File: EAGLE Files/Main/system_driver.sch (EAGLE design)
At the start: 11 parts

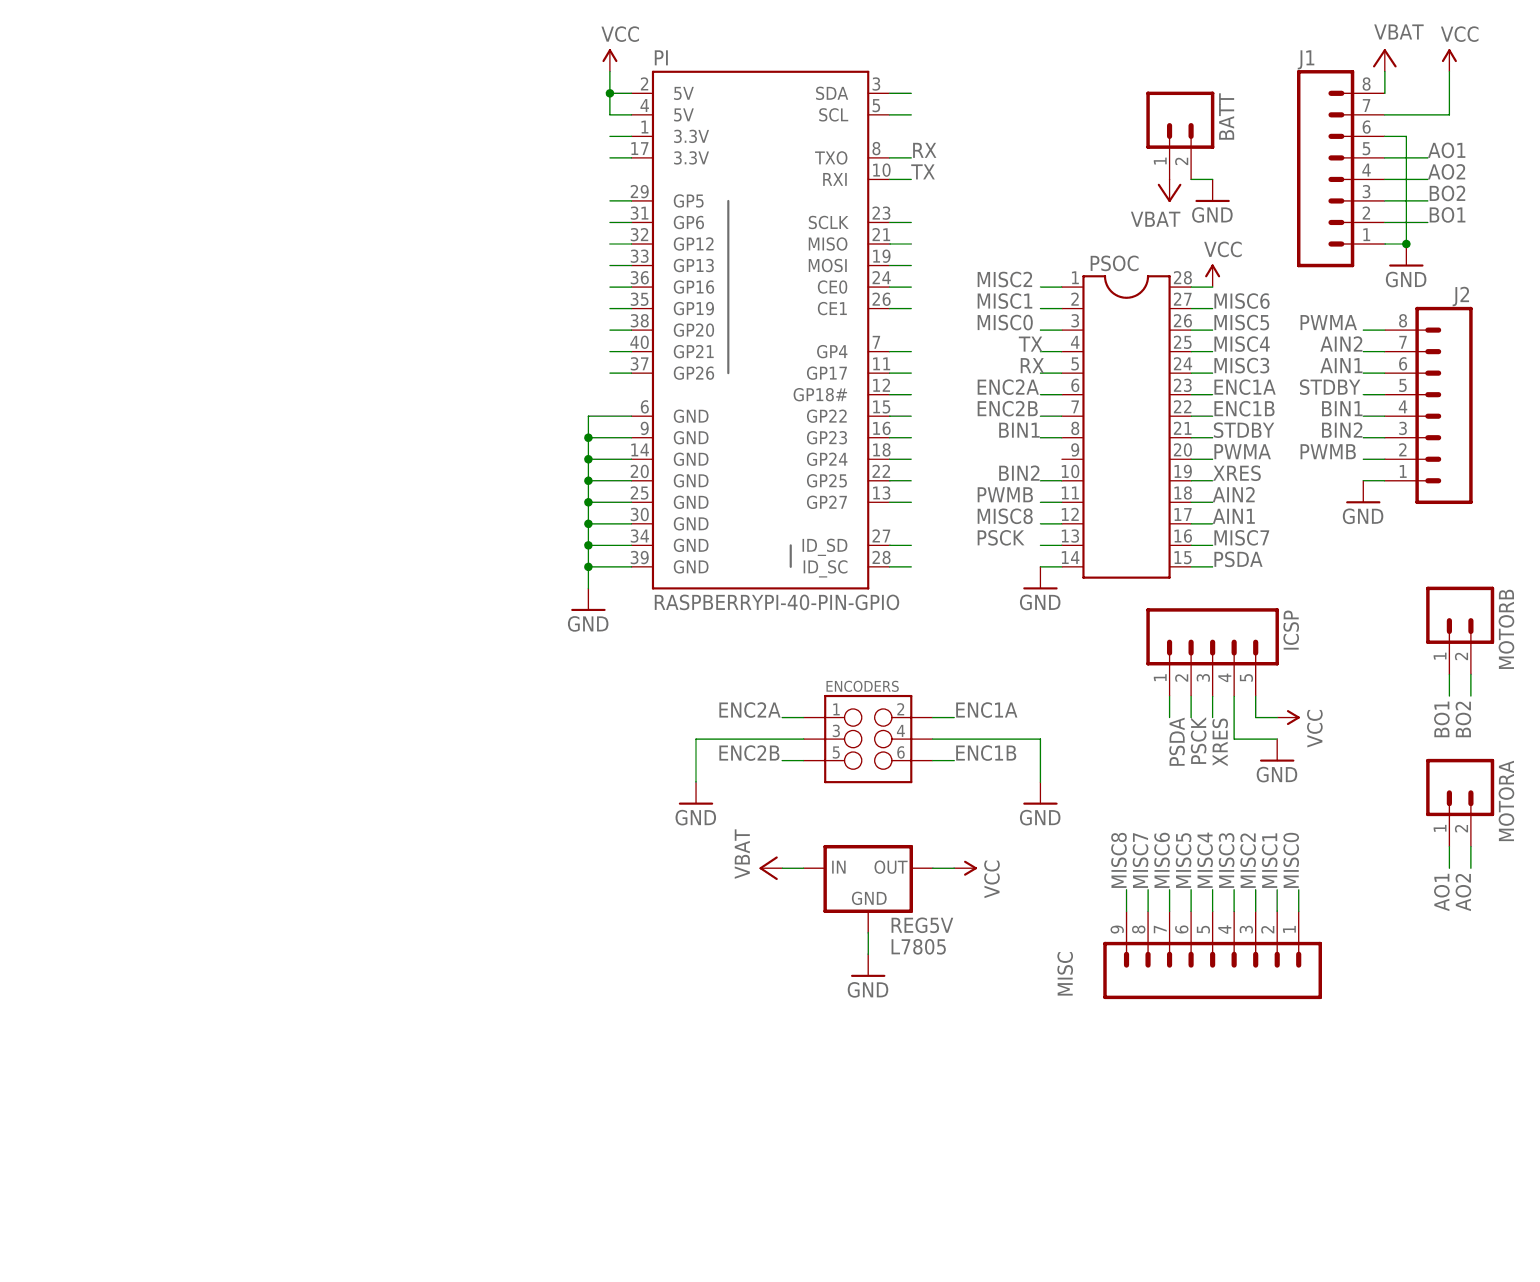
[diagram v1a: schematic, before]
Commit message: Updated PCB files, added PSoC code
Up to date PCB and schematic files for Robot 2's driver control board.
Also added the PSoC code files and project.
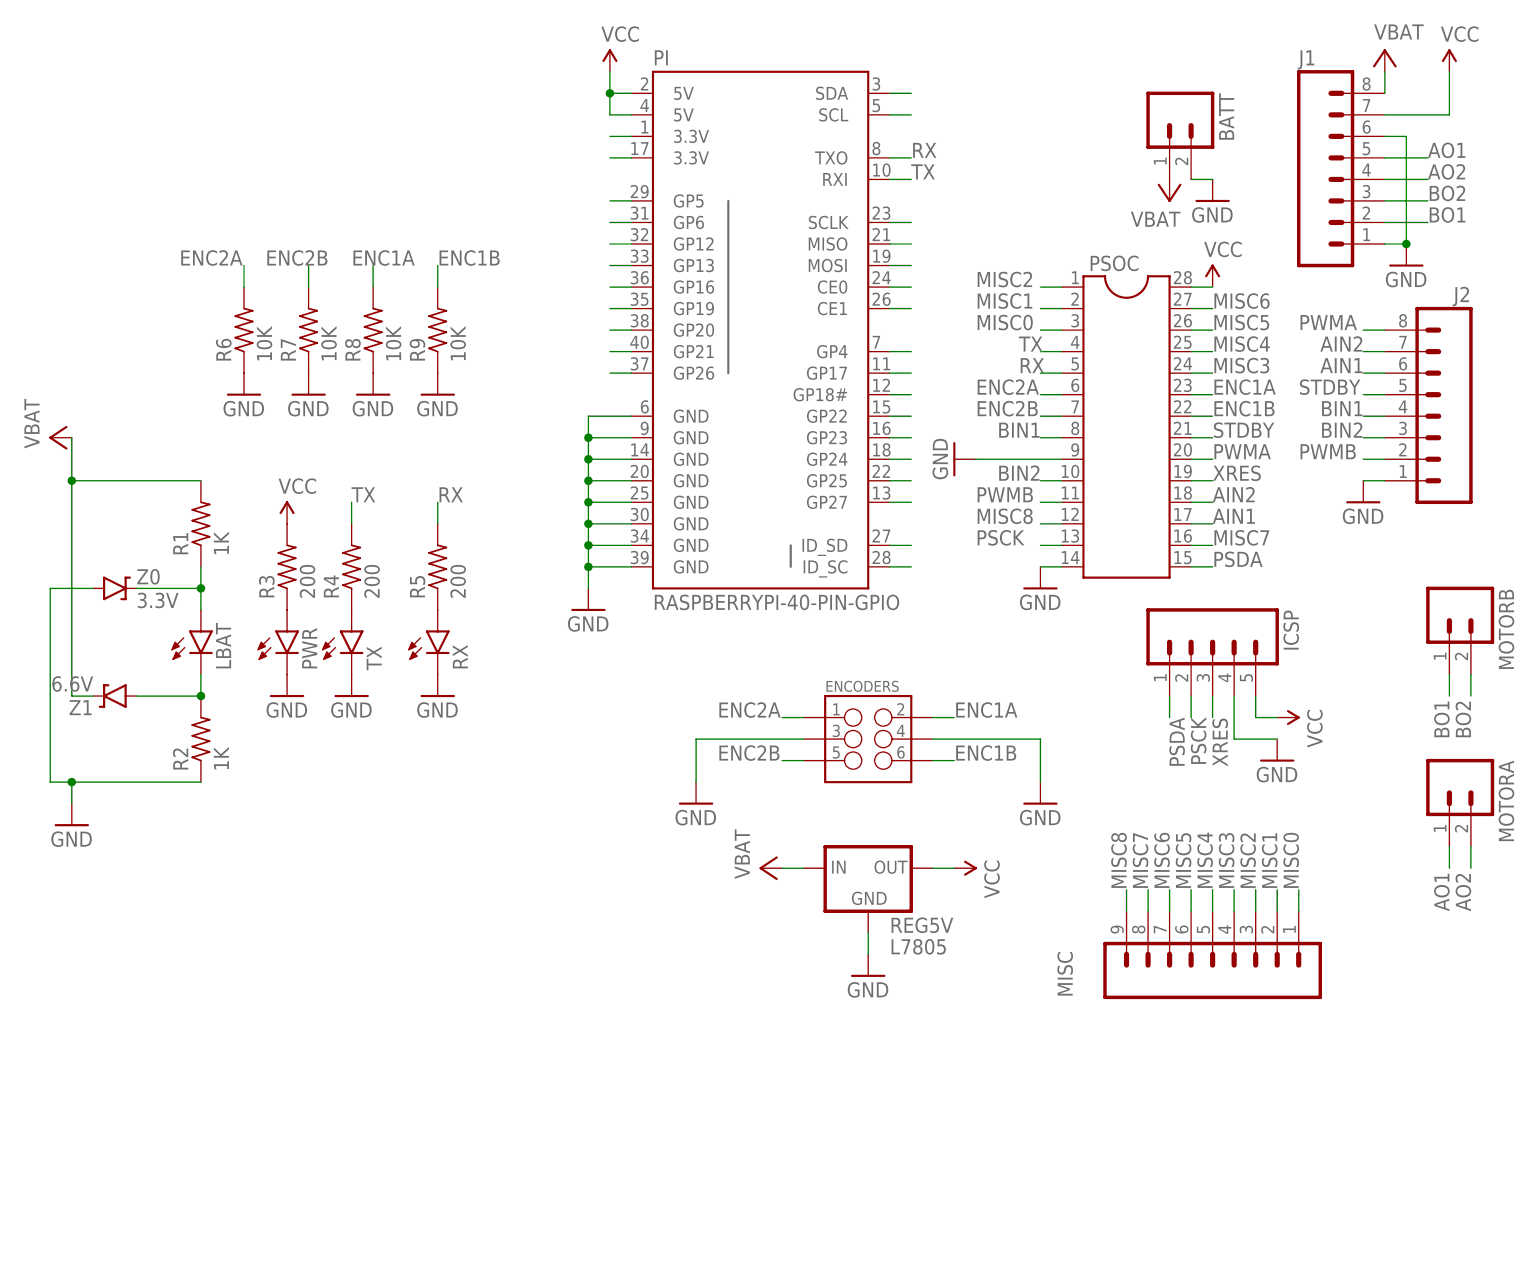
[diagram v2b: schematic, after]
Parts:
- added LBAT, PWR, RX, TX: (no value), SparkFun-LED:LED-FKIT-1206
- added R1, R2: 1K, resistor:R-US_M1206
- added R3, R4, R5: 200, resistor:R-US_M1206
- added R6, R7, R8, R9: 10K, resistor:R-US_M1206
- added Z0: 3.3V, SparkFun-DiscreteSemi:DIODE-ZENER16V
- added Z1: 6.6V, SparkFun-DiscreteSemi:DIODE-ZENER16V
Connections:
- new net N$1: LBAT.A, R1.1, Z0.C
- new net N$2: LBAT.C, R2.2, Z1.A
- new net N$3: PWR.A, R3.1
- new net N$4: R4.1, TX.A
- new net N$5: R5.1, RX.A
- net ENC1A: now also R8.2
- net ENC1B: now also R9.2
- net ENC2A: now also R6.2
- net ENC2B: now also R7.2
- net GND: now also PSOC.9, PWR.C, R2.1, R6.1, R7.1, R8.1, R9.1, RX.C, TX.C, Z0.A
- net RX: now also R5.2
- net TX: now also R4.2
- net V+: now also R1.2, Z1.C
- net VCC: now also R3.2
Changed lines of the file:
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@@
 <part name="VBAT2" library="supply2" deviceset="V+" device="" value="VBAT"/>
 <part name="SUPPLY7" library="SparkFun-Aesthetics" deviceset="VCC" device=""/>
+<part name="RX" library="SparkFun-LED" deviceset="LED" device="-FKIT-1206"/>
+<part name="TX" library="SparkFun-LED" deviceset="LED" device="-FKIT-1206"/>
+<part name="PWR" library="SparkFun-LED" deviceset="LED" device="-FKIT-1206"/>
+<part name="LBAT" library="SparkFun-LED" deviceset="LED" device="-FKIT-1206"/>
+<part name="R1" library="resistor" deviceset="R-US_" device="M1206" value="1K"/>
+<part name="R2" library="resistor" deviceset="R-US_" device="M1206" value="1K"/>
+<part name="Z1" library="SparkFun-DiscreteSemi" deviceset="DIODE-ZENER" device="16V" value="6.6V"/>
+<part name="Z0" library="SparkFun-DiscreteSemi" deviceset="DIODE-ZENER" device="16V" value="3.3V"/>
+<part name="GND7" library="SparkFun-Aesthetics" deviceset="GND" device=""/>
+<part name="VBAT3" library="supply2" deviceset="V+" device="" value="VBAT"/>
+<part name="R3" library="resistor" deviceset="R-US_" device="M1206" value="200"/>
+<part name="R4" library="resistor" deviceset="R-US_" device="M1206" value="200"/>
+<part name="R5" library="resistor" deviceset="R-US_" device="M1206" value="200"/>
+<part name="GND10" library="SparkFun-Aesthetics" deviceset="GND" device=""/>
+<part name="GND12" library="SparkFun-Aesthetics" deviceset="GND" device=""/>
+<part name="GND13" library="SparkFun-Aesthetics" deviceset="GND" device=""/>
+<part name="SUPPLY4" library="SparkFun-Aesthetics" deviceset="VCC" device=""/>
+<part name="GND14" library="SparkFun-Aesthetics" deviceset="GND" device=""/>
+<part name="GND15" library="SparkFun-Aesthetics" deviceset="GND" device=""/>
+<part name="GND16" library="SparkFun-Aesthetics" deviceset="GND" device=""/>
+<part name="GND17" library="SparkFun-Aesthetics" deviceset="GND" device=""/>
+<part name="GND18" library="SparkFun-Aesthetics" deviceset="GND" device=""/>
+<part name="R6" library="resistor" deviceset="R-US_" device="M1206" value="10K"/>
+<part name="R7" library="resistor" deviceset="R-US_" device="M1206" value="10K"/>
+<part name="R8" library="resistor" deviceset="R-US_" device="M1206" value="10K"/>
+<part name="R9" library="resistor" deviceset="R-US_" device="M1206" value="10K"/>
 </parts>
 <sheets>
@@
 <instance part="VBAT2" gate="1" x="-71.12" y="-15.24" rot="R90"/>
 <instance part="SUPPLY7" gate="G$1" x="-48.26" y="-15.24" rot="R270"/>
+<instance part="RX" gate="G$1" x="-109.22" y="12.7"/>
+<instance part="TX" gate="G$1" x="-119.38" y="12.7"/>
+<instance part="PWR" gate="G$1" x="-127" y="12.7"/>
+<instance part="LBAT" gate="G$1" x="-137.16" y="12.7"/>
+<instance part="R1" gate="G$1" x="-137.16" y="25.4" rot="R90"/>
+<instance part="R2" gate="G$1" x="-137.16" y="0" rot="R90"/>
+<instance part="Z1" gate="G$1" x="-147.32" y="5.08" rot="R180"/>
+<instance part="Z0" gate="G$1" x="-147.32" y="17.78"/>
+<instance part="GND7" gate="1" x="-152.4" y="-10.16"/>
+<instance part="VBAT3" gate="1" x="-154.94" y="35.56" rot="R90"/>
+<instance part="R3" gate="G$1" x="-127" y="20.32" rot="R90"/>
+<instance part="R4" gate="G$1" x="-119.38" y="20.32" rot="R90"/>
+<instance part="R5" gate="G$1" x="-109.22" y="20.32" rot="R90"/>
+<instance part="GND10" gate="1" x="-127" y="5.08"/>
+<instance part="GND12" gate="1" x="-119.38" y="5.08"/>
+<instance part="GND13" gate="1" x="-109.22" y="5.08"/>
+<instance part="SUPPLY4" gate="G$1" x="-127" y="25.4"/>
+<instance part="GND14" gate="1" x="-48.26" y="33.02" rot="R270"/>
+<instance part="GND15" gate="1" x="-109.22" y="40.64"/>
+<instance part="GND16" gate="1" x="-116.84" y="40.64"/>
+<instance part="GND17" gate="1" x="-124.46" y="40.64"/>
+<instance part="GND18" gate="1" x="-132.08" y="40.64"/>
+<instance part="R6" gate="G$1" x="-132.08" y="48.26" rot="R90"/>
+<instance part="R7" gate="G$1" x="-124.46" y="48.26" rot="R90"/>
+<instance part="R8" gate="G$1" x="-116.84" y="48.26" rot="R90"/>
+<instance part="R9" gate="G$1" x="-109.22" y="48.26" rot="R90"/>
 </instances>
 <busses>
@@
 <pinref part="SUPPLY7" gate="G$1" pin="VCC"/>
 <wire x1="-48.26" y1="-15.24" x2="-50.8" y2="-15.24" width="0.1524" layer="91"/>
+</segment>
+<segment>
+<pinref part="R3" gate="G$1" pin="2"/>
+<pinref part="SUPPLY4" gate="G$1" pin="VCC"/>
 </segment>
 </net>
@@
 <wire x1="-58.42" y1="-25.4" x2="-58.42" y2="-22.86" width="0.1524" layer="91"/>
 </segment>
+<segment>
+<pinref part="GND7" gate="1" pin="GND"/>
+<pinref part="R2" gate="G$1" pin="1"/>
+<wire x1="-152.4" y1="-5.08" x2="-152.4" y2="-7.62" width="0.1524" layer="91"/>
+<wire x1="-137.16" y1="-5.08" x2="-152.4" y2="-5.08" width="0.1524" layer="91"/>
+<pinref part="Z0" gate="G$1" pin="A"/>
+<wire x1="-149.86" y1="17.78" x2="-154.94" y2="17.78" width="0.1524" layer="91"/>
+<wire x1="-154.94" y1="17.78" x2="-154.94" y2="-5.08" width="0.1524" layer="91"/>
+<wire x1="-154.94" y1="-5.08" x2="-152.4" y2="-5.08" width="0.1524" layer="91"/>
+<junction x="-152.4" y="-5.08"/>
+</segment>
+<segment>
+<pinref part="PWR" gate="G$1" pin="C"/>
+<pinref part="GND10" gate="1" pin="GND"/>
+</segment>
+<segment>
+<pinref part="TX" gate="G$1" pin="C"/>
+<pinref part="GND12" gate="1" pin="GND"/>
+</segment>
+<segment>
+<pinref part="RX" gate="G$1" pin="C"/>
+<pinref part="GND13" gate="1" pin="GND"/>
+</segment>
+<segment>
+<pinref part="GND14" gate="1" pin="GND"/>
+<pinref part="PSOC" gate="G$1" pin="9"/>
+<wire x1="-45.72" y1="33.02" x2="-35.56" y2="33.02" width="0.1524" layer="91"/>
+</segment>
+<segment>
+<pinref part="GND18" gate="1" pin="GND"/>
+<pinref part="R6" gate="G$1" pin="1"/>
+</segment>
+<segment>
+<pinref part="GND17" gate="1" pin="GND"/>
+<pinref part="R7" gate="G$1" pin="1"/>
+</segment>
+<segment>
+<pinref part="GND16" gate="1" pin="GND"/>
+<pinref part="R8" gate="G$1" pin="1"/>
+</segment>
+<segment>
+<pinref part="GND15" gate="1" pin="GND"/>
+<pinref part="R9" gate="G$1" pin="1"/>
+</segment>
 </net>
 <net name="V+" class="0">
@@
 <wire x1="-68.58" y1="-15.24" x2="-66.04" y2="-15.24" width="0.1524" layer="91"/>
 </segment>
+<segment>
+<pinref part="VBAT3" gate="1" pin="V+"/>
+<pinref part="R1" gate="G$1" pin="2"/>
+<wire x1="-152.4" y1="30.48" x2="-152.4" y2="35.56" width="0.1524" layer="91"/>
+<wire x1="-137.16" y1="30.48" x2="-152.4" y2="30.48" width="0.1524" layer="91"/>
+<pinref part="Z1" gate="G$1" pin="C"/>
+<wire x1="-149.86" y1="5.08" x2="-152.4" y2="5.08" width="0.1524" layer="91"/>
+<wire x1="-152.4" y1="5.08" x2="-152.4" y2="30.48" width="0.1524" layer="91"/>
+<junction x="-152.4" y="30.48"/>
+</segment>
 </net>
 <net name="XRES" class="0">
@@
 <label x="-17.78" y="40.64" size="1.778" layer="95"/>
 </segment>
+<segment>
+<wire x1="-116.84" y1="53.34" x2="-116.84" y2="55.88" width="0.1524" layer="91"/>
+<label x="-119.38" y="55.88" size="1.778" layer="95"/>
+<pinref part="R8" gate="G$1" pin="2"/>
+</segment>
 </net>
 <net name="ENC1B" class="0">
@@
 <label x="-17.78" y="38.1" size="1.778" layer="95"/>
 </segment>
+<segment>
+<wire x1="-109.22" y1="53.34" x2="-109.22" y2="55.88" width="0.1524" layer="91"/>
+<label x="-109.22" y="55.88" size="1.778" layer="95"/>
+<pinref part="R9" gate="G$1" pin="2"/>
+</segment>
 </net>
 <net name="ENC2B" class="0">
@@
 <label x="-45.72" y="38.1" size="1.778" layer="95"/>
 </segment>
+<segment>
+<wire x1="-124.46" y1="53.34" x2="-124.46" y2="55.88" width="0.1524" layer="91"/>
+<label x="-129.54" y="55.88" size="1.778" layer="95"/>
+<pinref part="R7" gate="G$1" pin="2"/>
+</segment>
 </net>
 <net name="ENC2A" class="0">
@@
 <label x="-45.72" y="40.64" size="1.778" layer="95"/>
 </segment>
+<segment>
+<wire x1="-132.08" y1="53.34" x2="-132.08" y2="55.88" width="0.1524" layer="91"/>
+<label x="-139.7" y="55.88" size="1.778" layer="95"/>
+<pinref part="R6" gate="G$1" pin="2"/>
+</segment>
 </net>
 <net name="RX" class="0">
@@
 <label x="-53.34" y="68.58" size="1.778" layer="95"/>
 </segment>
+<segment>
+<pinref part="R5" gate="G$1" pin="2"/>
+<wire x1="-109.22" y1="25.4" x2="-109.22" y2="27.94" width="0.1524" layer="91"/>
+<label x="-109.22" y="27.94" size="1.778" layer="95"/>
+</segment>
 </net>
 <net name="TX" class="0">
@@
 <label x="-53.34" y="66.04" size="1.778" layer="95"/>
 </segment>
+<segment>
+<pinref part="R4" gate="G$1" pin="2"/>
+<wire x1="-119.38" y1="25.4" x2="-119.38" y2="27.94" width="0.1524" layer="91"/>
+<label x="-119.38" y="27.94" size="1.778" layer="95"/>
+</segment>
 </net>
 <net name="MISC0" class="0">
@@
 </segment>
 </net>
+<net name="N$1" class="0">
+<segment>
+<pinref part="LBAT" gate="G$1" pin="A"/>
+<pinref part="R1" gate="G$1" pin="1"/>
+<wire x1="-137.16" y1="20.32" x2="-137.16" y2="17.78" width="0.1524" layer="91"/>
+<pinref part="Z0" gate="G$1" pin="C"/>
+<wire x1="-137.16" y1="17.78" x2="-137.16" y2="15.24" width="0.1524" layer="91"/>
+<wire x1="-144.78" y1="17.78" x2="-137.16" y2="17.78" width="0.1524" layer="91"/>
+<junction x="-137.16" y="17.78"/>
+</segment>
+</net>
+<net name="N$2" class="0">
+<segment>
+<pinref part="R2" gate="G$1" pin="2"/>
+<pinref part="Z1" gate="G$1" pin="A"/>
+<wire x1="-144.78" y1="5.08" x2="-137.16" y2="5.08" width="0.1524" layer="91"/>
+<pinref part="LBAT" gate="G$1" pin="C"/>
+<wire x1="-137.16" y1="7.62" x2="-137.16" y2="5.08" width="0.1524" layer="91"/>
+<junction x="-137.16" y="5.08"/>
+</segment>
+</net>
+<net name="N$3" class="0">
+<segment>
+<pinref part="PWR" gate="G$1" pin="A"/>
+<pinref part="R3" gate="G$1" pin="1"/>
+</segment>
+</net>
+<net name="N$4" class="0">
+<segment>
+<pinref part="TX" gate="G$1" pin="A"/>
+<pinref part="R4" gate="G$1" pin="1"/>
+</segment>
+</net>
+<net name="N$5" class="0">
+<segment>
+<pinref part="RX" gate="G$1" pin="A"/>
+<pinref part="R5" gate="G$1" pin="1"/>
+</segment>
+</net>

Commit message: fixed merge issues?
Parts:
- added PWR_SW: (no value), SparkFun-Electromechanical:SWITCH-SPDTPTH
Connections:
- removed net MISO: PI.MISO
- removed net SCLK: PI.SCLK
- new net REGIN: J1.8, PWR_SW.P, R1.2, REG5V.IN, Z1.C
- net GND: now also PWR_SW.S
- net V+: now also PWR_SW.O; no longer J1.8, R1.2, REG5V.IN, Z1.C
